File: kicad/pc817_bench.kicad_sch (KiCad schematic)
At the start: 14 parts, among them J1 24V inputs, U1 PC817, U2 PC817

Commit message: Add the board: generated two-layer UNO shield layout
generate_pcb.py places and routes the parts with KiCad's pcbnew module, from
the netlist exported by the schematic. The Arduino footprint is flipped to
the back side so the shield is not mirrored. check.sh now builds and checks
both schematic and board (DRC: no errors, schematic parity OK, KiCad 10.0.6).
Schematic: footprints assigned; the GND pin next to AREF is left unconnected.

Co-Authored-By: Claude Fable 5.1 <noreply@anthropic.com>
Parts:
- A1: footprint (none) -> Module:Arduino_UNO_R3
- D1, D2: footprint (none) -> LED_THT:LED_D3.0mm
- D3, D4: footprint (none) -> Diode_THT:D_DO-35_SOD27_P7.62mm_Horizontal
- J1: footprint (none) -> TerminalBlock_Phoenix:TerminalBlock_Phoenix_MKDS-1,5-3_1x03_P5.00mm_Horizontal
- R1, R2, R3, R4, R5, R6: footprint (none) -> Resistor_THT:R_Axial_DIN0207_L6.3mm_D2.5mm_P10.16mm_Horizontal
- U1, U2: footprint (none) -> Package_DIP:DIP-4_W7.62mm
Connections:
- net D2: now also A1.17 (D2); no longer A1.D2
- net D3: now also A1.18 (D3); no longer A1.D3
- net GND: now also A1.6 (GND), A1.7 (GND); no longer A1.GND1 (GND), A1.GND2 (GND), A1.GND3 (GND)
- net IOREF: now also A1.2 (IOREF); no longer A1.IOREF
- no-connect marks 26 -> 27
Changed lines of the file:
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@@
 (kicad_sch (version 20230121) (generator eeschema)
   (paper "A4")
-  (title_block (title "PC817 24 V input test bench") (date "2026-10-02") (rev "0.4")
+  (title_block (title "PC817 24 V input test bench") (date "2026-10-02") (rev "0.5")
     (comment 1 "Generated by generate.py - edit the script, not this file"))
   (symbol (lib_id "bench:R_H") (at 71.12 71.12 0) (unit 1) (in_bom yes) (on_board yes) (dnp no)
     (property "Reference" "R1" (at 71.12 66.04 0) (effects (font (size 1.27 1.27))))
     (property "Value" "2.2k" (at 71.12 68.58 0) (effects (font (size 1.27 1.27))))
-    (property "Footprint" "" (at 71.12 71.12 0) (effects (font (size 1.27 1.27)) hide))
+    (property "Footprint" "Resistor_THT:R_Axial_DIN0207_L6.3mm_D2.5mm_P10.16mm_Horizontal" (at 71.12 71.12 0) (effects (font (size 1.27 1.27)) hide))
     (property "Datasheet" "" (at 71.12 71.12 0) (effects (font (size 1.27 1.27)) hide))
     (pin "1") (pin "2")
@@
     (property "Reference" "R2" (at 81.28 66.04 0) (effects (font (size 1.27 1.27))))
     (property "Value" "2.2k" (at 81.28 68.58 0) (effects (font (size 1.27 1.27))))
-    (property "Footprint" "" (at 81.28 71.12 0) (effects (font (size 1.27 1.27)) hide))
+    (property "Footprint" "Resistor_THT:R_Axial_DIN0207_L6.3mm_D2.5mm_P10.16mm_Horizontal" (at 81.28 71.12 0) (effects (font (size 1.27 1.27)) hide))
     (property "Datasheet" "" (at 81.28 71.12 0) (effects (font (size 1.27 1.27)) hide))
     (pin "1") (pin "2")
@@
     (property "Reference" "D1" (at 97.79 66.04 0) (effects (font (size 1.27 1.27))))
     (property "Value" "LED red" (at 97.79 74.93 0) (effects (font (size 1.27 1.27))))
-    (property "Footprint" "" (at 97.79 71.12 0) (effects (font (size 1.27 1.27)) hide))
+    (property "Footprint" "LED_THT:LED_D3.0mm" (at 97.79 71.12 0) (effects (font (size 1.27 1.27)) hide))
     (property "Datasheet" "" (at 97.79 71.12 0) (effects (font (size 1.27 1.27)) hide))
     (pin "2") (pin "1")
@@
     (property "Reference" "D3" (at 83.82 73.66 0) (effects (font (size 1.27 1.27))))
     (property "Value" "1N4148" (at 83.82 76.2 0) (effects (font (size 1.27 1.27))))
-    (property "Footprint" "" (at 88.9 74.93 0) (effects (font (size 1.27 1.27)) hide))
+    (property "Footprint" "Diode_THT:D_DO-35_SOD27_P7.62mm_Horizontal" (at 88.9 74.93 0) (effects (font (size 1.27 1.27)) hide))
     (property "Datasheet" "" (at 88.9 74.93 0) (effects (font (size 1.27 1.27)) hide))
     (pin "1") (pin "2")
@@
     (property "Reference" "U1" (at 115.57 66.04 0) (effects (font (size 1.27 1.27))))
     (property "Value" "PC817" (at 115.57 81.28 0) (effects (font (size 1.27 1.27))))
-    (property "Footprint" "" (at 119.38 73.66 0) (effects (font (size 1.27 1.27)) hide))
+    (property "Footprint" "Package_DIP:DIP-4_W7.62mm" (at 119.38 73.66 0) (effects (font (size 1.27 1.27)) hide))
     (property "Datasheet" "" (at 119.38 73.66 0) (effects (font (size 1.27 1.27)) hide))
     (pin "1") (pin "2") (pin "4") (pin "3")
@@
     (property "Reference" "R5" (at 140.97 63.5 0) (effects (font (size 1.27 1.27))))
     (property "Value" "10k" (at 140.97 66.04 0) (effects (font (size 1.27 1.27))))
-    (property "Footprint" "" (at 137.16 64.77 0) (effects (font (size 1.27 1.27)) hide))
+    (property "Footprint" "Resistor_THT:R_Axial_DIN0207_L6.3mm_D2.5mm_P10.16mm_Horizontal" (at 137.16 64.77 0) (effects (font (size 1.27 1.27)) hide))
     (property "Datasheet" "" (at 137.16 64.77 0) (effects (font (size 1.27 1.27)) hide))
     (pin "1") (pin "2")
@@
     (property "Reference" "R3" (at 71.12 116.84 0) (effects (font (size 1.27 1.27))))
     (property "Value" "2.2k" (at 71.12 119.38 0) (effects (font (size 1.27 1.27))))
-    (property "Footprint" "" (at 71.12 121.92 0) (effects (font (size 1.27 1.27)) hide))
+    (property "Footprint" "Resistor_THT:R_Axial_DIN0207_L6.3mm_D2.5mm_P10.16mm_Horizontal" (at 71.12 121.92 0) (effects (font (size 1.27 1.27)) hide))
     (property "Datasheet" "" (at 71.12 121.92 0) (effects (font (size 1.27 1.27)) hide))
     (pin "1") (pin "2")
@@
     (property "Reference" "R4" (at 81.28 116.84 0) (effects (font (size 1.27 1.27))))
     (property "Value" "2.2k" (at 81.28 119.38 0) (effects (font (size 1.27 1.27))))
-    (property "Footprint" "" (at 81.28 121.92 0) (effects (font (size 1.27 1.27)) hide))
+    (property "Footprint" "Resistor_THT:R_Axial_DIN0207_L6.3mm_D2.5mm_P10.16mm_Horizontal" (at 81.28 121.92 0) (effects (font (size 1.27 1.27)) hide))
     (property "Datasheet" "" (at 81.28 121.92 0) (effects (font (size 1.27 1.27)) hide))
     (pin "1") (pin "2")
@@
     (property "Reference" "D2" (at 97.79 116.84 0) (effects (font (size 1.27 1.27))))
     (property "Value" "LED red" (at 97.79 125.73 0) (effects (font (size 1.27 1.27))))
-    (property "Footprint" "" (at 97.79 121.92 0) (effects (font (size 1.27 1.27)) hide))
+    (property "Footprint" "LED_THT:LED_D3.0mm" (at 97.79 121.92 0) (effects (font (size 1.27 1.27)) hide))
     (property "Datasheet" "" (at 97.79 121.92 0) (effects (font (size 1.27 1.27)) hide))
     (pin "2") (pin "1")
@@
     (property "Reference" "D4" (at 83.82 124.46 0) (effects (font (size 1.27 1.27))))
     (property "Value" "1N4148" (at 83.82 127 0) (effects (font (size 1.27 1.27))))
-    (property "Footprint" "" (at 88.9 125.73 0) (effects (font (size 1.27 1.27)) hide))
+    (property "Footprint" "Diode_THT:D_DO-35_SOD27_P7.62mm_Horizontal" (at 88.9 125.73 0) (effects (font (size 1.27 1.27)) hide))
     (property "Datasheet" "" (at 88.9 125.73 0) (effects (font (size 1.27 1.27)) hide))
     (pin "1") (pin "2")
@@
     (property "Reference" "U2" (at 115.57 116.84 0) (effects (font (size 1.27 1.27))))
     (property "Value" "PC817" (at 115.57 132.08 0) (effects (font (size 1.27 1.27))))
-    (property "Footprint" "" (at 119.38 124.46 0) (effects (font (size 1.27 1.27)) hide))
+    (property "Footprint" "Package_DIP:DIP-4_W7.62mm" (at 119.38 124.46 0) (effects (font (size 1.27 1.27)) hide))
     (property "Datasheet" "" (at 119.38 124.46 0) (effects (font (size 1.27 1.27)) hide))
     (pin "1") (pin "2") (pin "4") (pin "3")
@@
     (property "Reference" "R6" (at 140.97 114.3 0) (effects (font (size 1.27 1.27))))
     (property "Value" "10k" (at 140.97 116.84 0) (effects (font (size 1.27 1.27))))
-    (property "Footprint" "" (at 137.16 115.57 0) (effects (font (size 1.27 1.27)) hide))
+    (property "Footprint" "Resistor_THT:R_Axial_DIN0207_L6.3mm_D2.5mm_P10.16mm_Horizontal" (at 137.16 115.57 0) (effects (font (size 1.27 1.27)) hide))
     (property "Datasheet" "" (at 137.16 115.57 0) (effects (font (size 1.27 1.27)) hide))
     (pin "1") (pin "2")
@@
     (property "Reference" "J1" (at 29.21 88.9 0) (effects (font (size 1.27 1.27))))
     (property "Value" "24V inputs" (at 29.21 104.14 0) (effects (font (size 1.27 1.27))))
-    (property "Footprint" "" (at 30.48 96.52 0) (effects (font (size 1.27 1.27)) hide))
+    (property "Footprint" "TerminalBlock_Phoenix:TerminalBlock_Phoenix_MKDS-1,5-3_1x03_P5.00mm_Horizontal" (at 30.48 96.52 0) (effects (font (size 1.27 1.27)) hide))
     (property "Datasheet" "" (at 30.48 96.52 0) (effects (font (size 1.27 1.27)) hide))
     (pin "1") (pin "2") (pin "3")
@@
     (property "Reference" "A1" (at 200.66 69.85 0) (effects (font (size 1.27 1.27))))
     (property "Value" "UNO R4 WiFi or UNO Q" (at 200.66 123.19 0) (effects (font (size 1.27 1.27))))
-    (property "Footprint" "" (at 200.66 96.52 0) (effects (font (size 1.27 1.27)) hide))
+    (property "Footprint" "Module:Arduino_UNO_R3" (at 200.66 96.52 0) (effects (font (size 1.27 1.27)) hide))
     (property "Datasheet" "" (at 200.66 96.52 0) (effects (font (size 1.27 1.27)) hide))
-    (pin "NC") (pin "IOREF") (pin "RESET") (pin "3V3") (pin "5V") (pin "GND1") (pin "GND2") (pin "VIN") (pin "A0") (pin "A1") (pin "A2") (pin "A3") (pin "A4") (pin "A5") (pin "SCL") (pin "SDA") (pin "AREF") (pin "GND3") (pin "D13") (pin "D12") (pin "D11") (pin "D10") (pin "D9") (pin "D8") (pin "D7") (pin "D6") (pin "D5") (pin "D4") (pin "D3") (pin "D2") (pin "D1") (pin "D0")
+    (pin "1") (pin "2") (pin "3") (pin "4") (pin "5") (pin "6") (pin "7") (pin "8") (pin "9") (pin "10") (pin "11") (pin "12") (pin "13") (pin "14") (pin "32") (pin "31") (pin "30") (pin "29") (pin "28") (pin "27") (pin "26") (pin "25") (pin "24") (pin "23") (pin "22") (pin "21") (pin "20") (pin "19") (pin "18") (pin "17") (pin "16") (pin "15")
     (instances (project "pc817_bench" (path "/6f1d2c1e-0a4b-4c55-9a51-2b8f0c817001" (reference "A1") (unit 1)))))
   (no_connect (at 185.42 74.93))
@@
   (no_connect (at 215.9 77.47))
   (no_connect (at 215.9 80.01))
-  (wire (pts (xy 215.9 82.55) (xy 226.06 82.55)) (stroke (width 0) (type default)))
-  (label "GND" (at 226.06 82.55 0) (effects (font (size 1.27 1.27)) (justify right bottom)))
+  (no_connect (at 215.9 82.55))
   (no_connect (at 215.9 85.09))
   (no_connect (at 215.9 87.63))

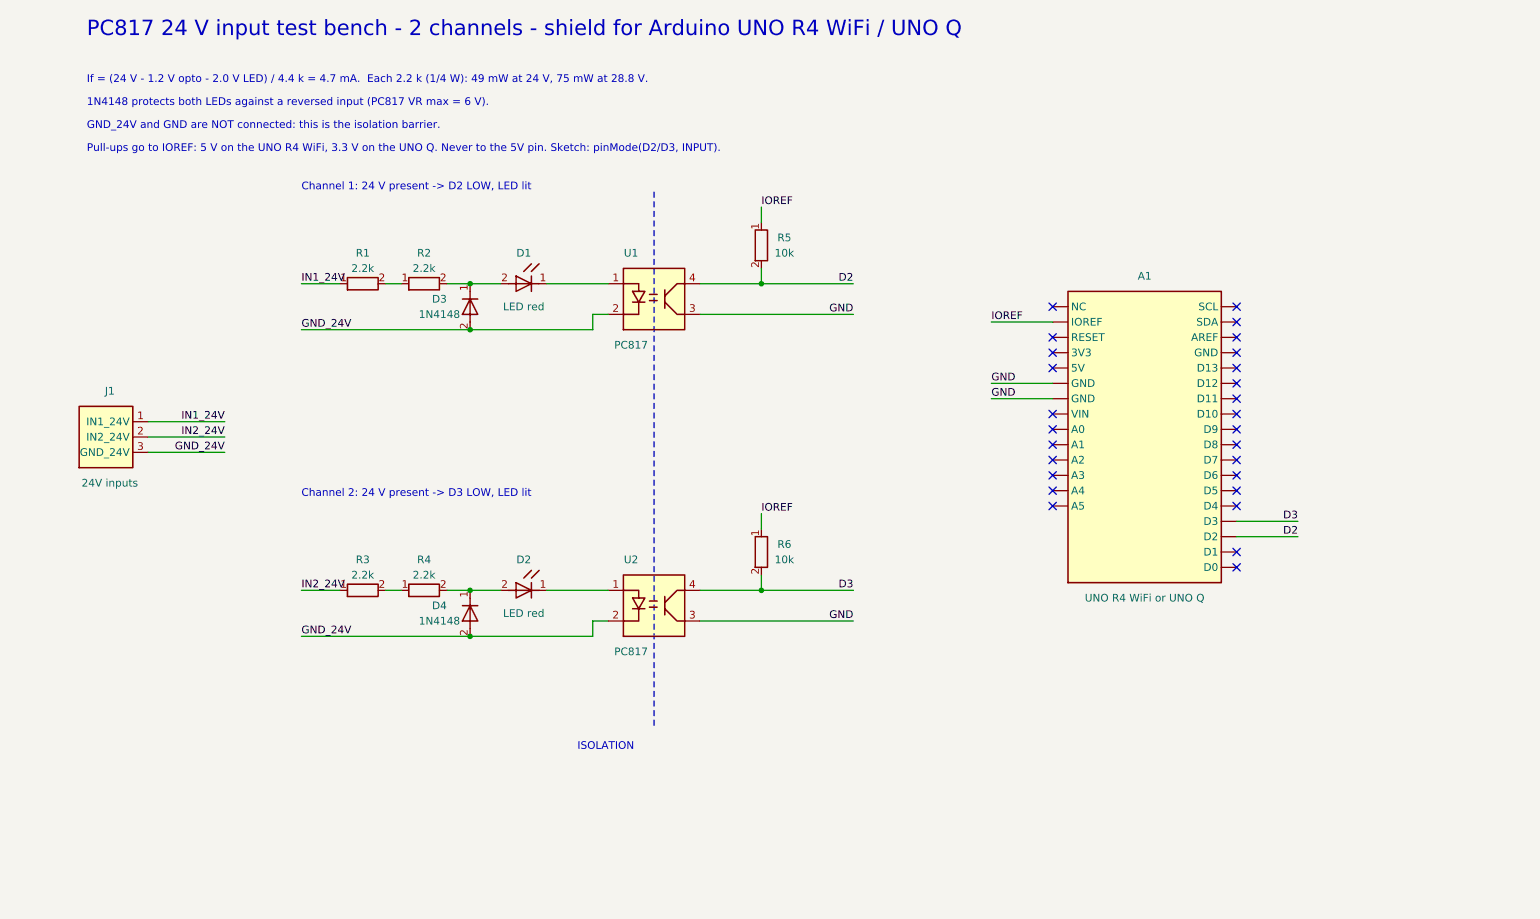
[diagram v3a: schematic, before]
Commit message: Two e-stop loops: fused 24 V out to each button, return through the PC817 channel
J1 is now a 6-way terminal (24V, ES1+, ES1, ES2+, ES2, 0V) and F1 (T2A) protects
the 24 V leaving the board. Series resistors 2 x 1.5k: 6.9 mA loop current.
Board re-routed; DRC: no errors, schematic parity OK (KiCad 10.0.6).

Co-Authored-By: Claude Fable 5.1 <noreply@anthropic.com>
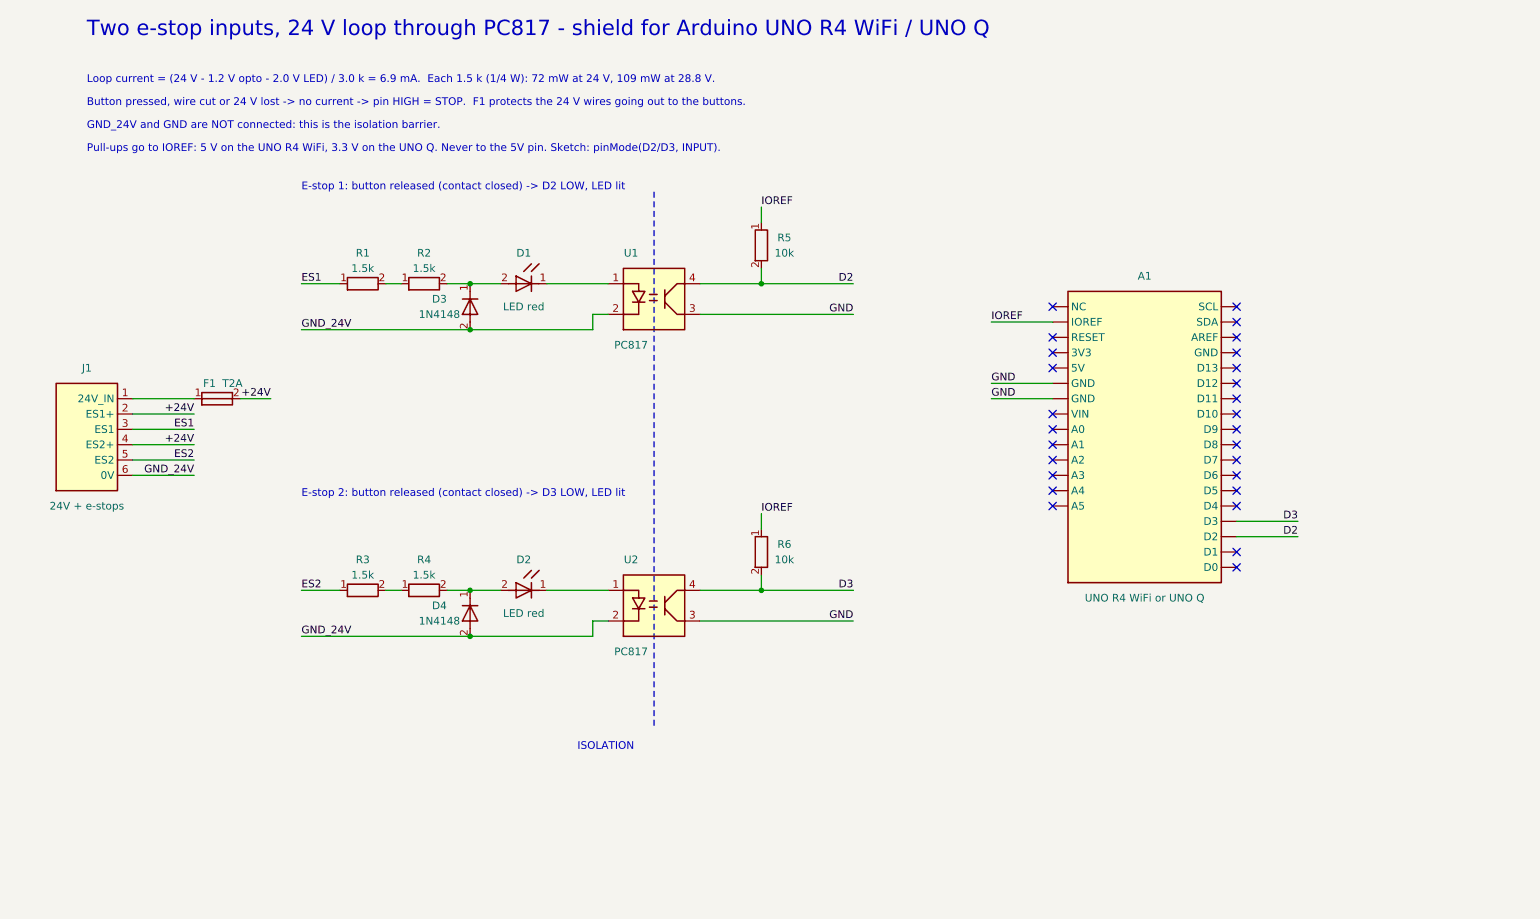
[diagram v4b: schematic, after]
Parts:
- removed J1: 24V inputs, TerminalBlock_Phoenix:TerminalBlock_Phoenix_MKDS-1,5-3_1x03_P5.00mm_Horizontal, symbol bench:CONN3
- added F1: T2A, Fuse:Fuse_Littelfuse_372_D8.50mm, symbol bench:FUSE_H
- added J1: 24V + e-stops, TerminalBlock_Phoenix:TerminalBlock_Phoenix_MKDS-1,5-6_1x06_P5.00mm_Horizontal, symbol bench:CONN6
- R1, R2, R3, R4: value 2.2k -> 1.5k
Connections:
- net GND_24V: now also J1.6 (0V)
- net IN1_24V renamed ES1
- net ES1: now also J1.3 (ES1)
- net IN2_24V renamed ES2
- net ES2: now also J1.5 (ES2)
- new net: F1.1, J1.1 (24V_IN)
- new net +24V: F1.2, J1.2 (ES1+), J1.4 (ES2+)
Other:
- note added: "Button pressed, wire cut or 24 V lost -> no current -> pin HIGH = STOP. F1 protects the 24 V wires going out to the buttons."
- note added: "E-stop 1: button released (contact closed) -> D2 LOW, LED lit"
- note added: "E-stop 2: button released (contact closed) -> D3 LOW, LED lit"
- note added: "Loop current = (24 V - 1.2 V opto - 2.0 V LED) / 3.0 k = 6.9 mA. Each 1.5 k (1/4 W): 72 mW at 24 V, 109 mW at 28.8 V."
- note added: "Two e-stop inputs, 24 V loop through PC817 - shield for Arduino UNO R4 WiFi / UNO Q"
- note removed: "1N4148 protects both LEDs against a reversed input (PC817 VR max = 6 V)."
- note removed: "Channel 1: 24 V present -> D2 LOW, LED lit"
- note removed: "Channel 2: 24 V present -> D3 LOW, LED lit"
- note removed: "If = (24 V - 1.2 V opto - 2.0 V LED) / 4.4 k = 4.7 mA. Each 2.2 k (1/4 W): 49 mW at 24 V, 75 mW at 28.8 V."
- note removed: "PC817 24 V input test bench - 2 channels - shield for Arduino UNO R4 WiFi / UNO Q"
- title: PC817 24 V input test bench -> E-stop inputs: 24 V loop through PC817
